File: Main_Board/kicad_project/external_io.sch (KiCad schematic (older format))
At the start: 19 parts, among them J19 I2C_BUFFERED, J20 USB_B_Micro, J21 DATA_UART, J22 I2C_EXTERNAL, U8 PCA9600DP, U9 USBLC6-2SC6

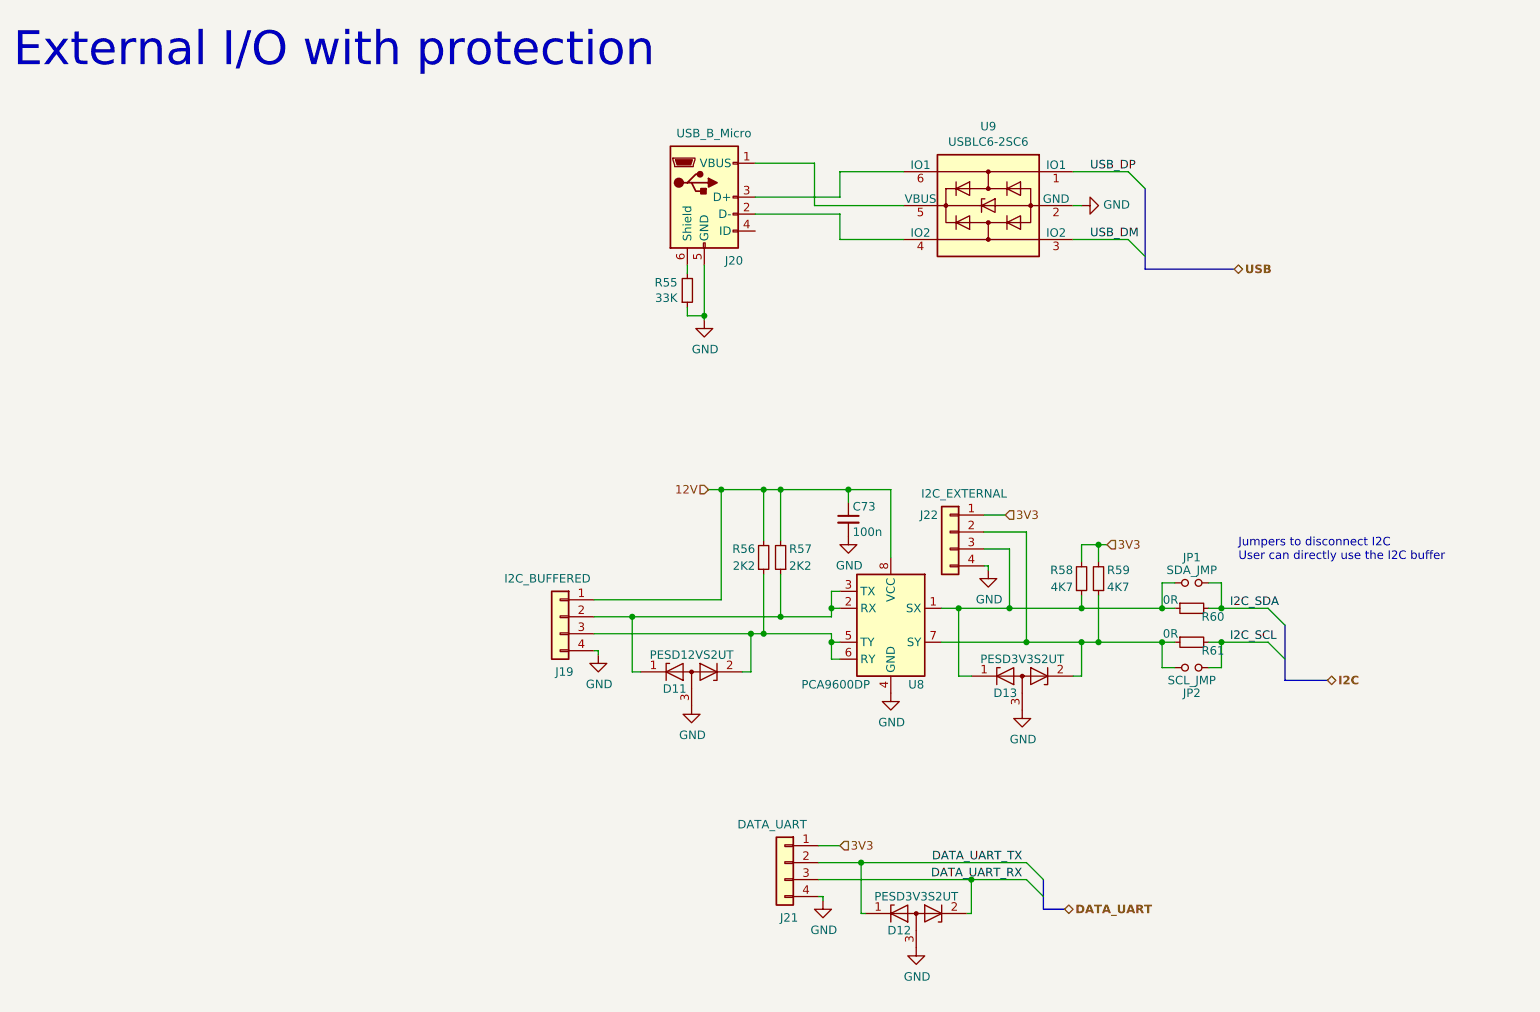
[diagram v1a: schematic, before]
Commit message: progress on MCU pinout
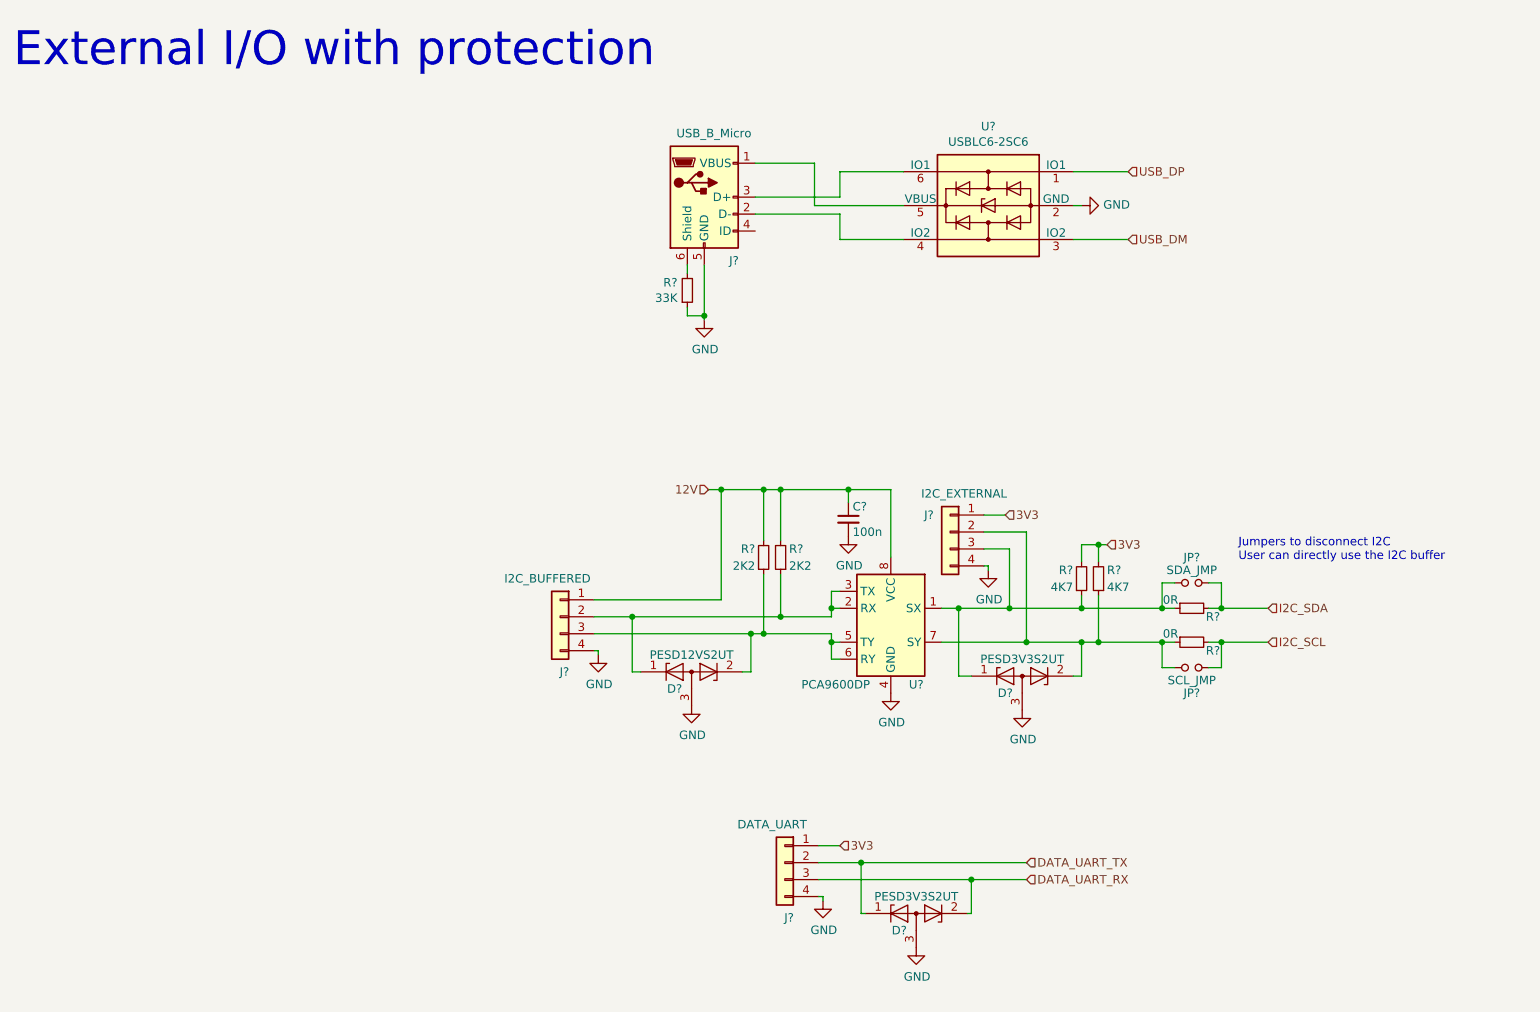
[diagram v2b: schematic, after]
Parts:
- renumbered C73 to C?, D11 to D?, D12 to D?, D13 to D?, J20 to J?, J22 to J?, J19 to J?, J21 to J?, JP1 to JP?, JP2 to JP?, R55 to R?, R60 to R?, R61 to R?, R58 to R?, R59 to R?, R57 to R?, R56 to R?, U8 to U?, U9 to U?
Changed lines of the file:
@@
 $EndDescr
 $Comp
-L Interface:PCA9600DP U8
+L Interface:PCA9600DP U?
 U 1 1 5F70BE3C
 P 5875 4200
-F 0 "U8" H 5725 3850 50  0000 C CNN
+F 0 "U?" H 5725 3850 50  0000 C CNN
 F 1 "PCA9600DP" H 6200 3850 50  0000 C CNN
 F 2 "Package_SO:TSSOP-8_3x3mm_P0.65mm" H 6675 3850 50  0001 C CNN
@@
 $EndComp
 $Comp
-L Connector:USB_B_Micro J20
+L Connector:USB_B_Micro J?
 U 1 1 5F70DEC7
 P 4775 1675
-F 0 "J20" H 4950 1300 50  0000 C CNN
+F 0 "J?" H 4950 1300 50  0000 C CNN
 F 1 "USB_B_Micro" H 4832 2051 50  0000 C CNN
 F 2 "Connector_USB:USB_Micro-B_Molex_47346-0001" H 4925 1625 50  0001 C CNN
@@
 $EndComp
 $Comp
-L LoaDy:USBLC6-2SC6 U9
+L LoaDy:USBLC6-2SC6 U?
 U 1 1 5F71A98E
 P 6450 1725
-F 0 "U9" H 6450 2192 50  0000 C CNN
+F 0 "U?" H 6450 2192 50  0000 C CNN
 F 1 "USBLC6-2SC6" H 6450 2101 50  0000 C CNN
 F 2 "Package_TO_SOT_SMD:SOT-23-6" H 7275 2125 50  0001 C CNN
@@
 $EndComp
 $Comp
-L power:GND #PWR081
+L power:GND #PWR?
 U 1 1 5F71E77C
 P 4775 2400
-F 0 "#PWR081" H 4775 2150 50  0001 C CNN
+F 0 "#PWR?" H 4775 2150 50  0001 C CNN
 F 1 "GND" H 4780 2227 50  0000 C CNN
 F 2 "" H 4775 2400 50  0001 C CNN
@@
 	5425 1725 5425 1475
 $Comp
-L Device:R_Small R55
+L Device:R_Small R?
 U 1 1 5F7222AA
 P 4675 2225
-F 0 "R55" H 4617 2179 50  0000 R CNN
+F 0 "R?" H 4617 2179 50  0000 R CNN
 F 1 "33K" H 4617 2270 50  0000 R CNN
 F 2 "Resistor_SMD:R_0603_1608Metric" H 4675 2225 50  0001 C CNN
@@
 	4675 2125 4675 2075
 $Comp
-L power:GND #PWR088
+L power:GND #PWR?
 U 1 1 5F72339E
 P 7000 1725
-F 0 "#PWR088" H 7000 1475 50  0001 C CNN
+F 0 "#PWR?" H 7000 1475 50  0001 C CNN
 F 1 "GND" V 7005 1597 50  0000 R CNN
 F 2 "" H 7000 1725 50  0001 C CNN
@@
 Wire Wire Line
 	7000 1725 6950 1725
-Entry Wire Line
-	7275 1525 7375 1625
-Entry Wire Line
-	7275 1925 7375 2025
-Wire Bus Line
-	7375 2100 7900 2100
-Text HLabel 7900 2100 2    50   BiDi ~ 10
-USB
 Wire Wire Line
 	6950 1525 7275 1525
 Wire Wire Line
 	6950 1925 7275 1925
-Text Label 7050 1925 0    50   ~ 0
-USB_DM
-Text Label 7050 1525 0    50   ~ 0
-USB_DP
-$Comp
-L Device:R_Small R60
+$Comp
+L Device:R_Small R?
 U 1 1 5F728398
 P 7650 4100
-F 0 "R60" V 7700 3975 50  0000 C CNN
+F 0 "R?" V 7700 3975 50  0000 C CNN
 F 1 "0R" V 7600 4225 50  0000 C CNN
 F 2 "Resistor_SMD:R_0603_1608Metric" H 7650 4100 50  0001 C CNN
@@
 $EndComp
 $Comp
-L Device:R_Small R61
+L Device:R_Small R?
 U 1 1 5F728F58
 P 7650 4300
-F 0 "R61" V 7700 4175 50  0000 C CNN
+F 0 "R?" V 7700 4175 50  0000 C CNN
 F 1 "0R" V 7600 4425 50  0000 C CNN
 F 2 "Resistor_SMD:R_0603_1608Metric" H 7650 4300 50  0001 C CNN
@@
 	7550 4300 7475 4300
 $Comp
-L Device:Jumper_NO_Small JP1
+L Device:Jumper_NO_Small JP?
 U 1 1 5F730E54
 P 7650 3950
-F 0 "JP1" H 7650 4100 50  0000 C CNN
+F 0 "JP?" H 7650 4100 50  0000 C CNN
 F 1 "SDA_JMP" H 7650 4025 50  0000 C CNN
 F 2 "Connector_PinHeader_2.54mm:PinHeader_1x02_P2.54mm_Vertical" H 7650 3950 50  0001 C CNN
@@
 $EndComp
 $Comp
-L Device:Jumper_NO_Small JP2
+L Device:Jumper_NO_Small JP?
 U 1 1 5F7312C9
 P 7650 4450
-F 0 "JP2" H 7650 4600 50  0000 C CNN
+F 0 "JP?" H 7650 4600 50  0000 C CNN
 F 1 "SCL_JMP" H 7650 4525 50  0000 C CNN
 F 2 "Connector_PinHeader_2.54mm:PinHeader_1x02_P2.54mm_Vertical" H 7650 4450 50  0001 C CNN
@@
 3V3
 $Comp
-L power:GND #PWR086
+L power:GND #PWR?
 U 1 1 5F72CC53
 P 6450 3875
-F 0 "#PWR086" H 6450 3625 50  0001 C CNN
+F 0 "#PWR?" H 6450 3625 50  0001 C CNN
 F 1 "GND" H 6455 3702 50  0000 C CNN
 F 2 "" H 6450 3875 50  0001 C CNN
@@
 $EndComp
 $Comp
-L Connector_Generic:Conn_01x04 J22
+L Connector_Generic:Conn_01x04 J?
 U 1 1 5F729670
 P 6225 3650
-F 0 "J22" H 6350 3750 50  0000 C CNN
+F 0 "J?" H 6350 3750 50  0000 C CNN
 F 1 "I2C_EXTERNAL" H 6143 3876 50  0000 C CNN
 F 2 "Connector_PinHeader_2.54mm:PinHeader_1x04_P2.54mm_Vertical" H 6225 3650 50  0001 C CNN
@@
 	6675 4300 7000 4300
 $Comp
-L Device:R_Small R58
+L Device:R_Small R?
 U 1 1 5F74371A
 P 7000 3925
-F 0 "R58" H 6950 3875 50  0000 R CNN
+F 0 "R?" H 6950 3875 50  0000 R CNN
 F 1 "4K7" H 6950 3975 50  0000 R CNN
 F 2 "Resistor_SMD:R_0603_1608Metric" H 7000 3925 50  0001 C CNN
@@
 $EndComp
 $Comp
-L Device:R_Small R59
+L Device:R_Small R?
 U 1 1 5F743EA7
 P 7100 3925
-F 0 "R59" H 7050 3875 50  0000 R CNN
+F 0 "R?" H 7050 3875 50  0000 R CNN
 F 1 "4K7" H 7050 3975 50  0000 R CNN
 F 2 "Resistor_SMD:R_0603_1608Metric" H 7100 3925 50  0001 C CNN
@@
 Connection ~ 7100 3725
 $Comp
-L power:GND #PWR084
+L power:GND #PWR?
 U 1 1 5F747299
 P 5875 4600
-F 0 "#PWR084" H 5875 4350 50  0001 C CNN
+F 0 "#PWR?" H 5875 4350 50  0001 C CNN
 F 1 "GND" H 5880 4427 50  0000 C CNN
 F 2 "" H 5875 4600 50  0001 C CNN
@@
 $EndComp
 $Comp
-L Connector_Generic:Conn_01x04 J19
+L Connector_Generic:Conn_01x04 J?
 U 1 1 5F7475E6
 P 3925 4150
-F 0 "J19" H 3900 3825 50  0000 C CNN
+F 0 "J?" H 3900 3825 50  0000 C CNN
 F 1 "I2C_BUFFERED" H 4000 4375 50  0000 C CNN
 F 2 "Connector_PinHeader_2.54mm:PinHeader_1x04_P2.54mm_Horizontal" H 3925 4150 50  0001 C CNN
@@
 Connection ~ 5525 4100
 $Comp
-L Device:C_Small C73
+L Device:C_Small C?
 U 1 1 5F74C7A6
 P 5625 3575
-F 0 "C73" H 5650 3650 50  0000 L CNN
+F 0 "C?" H 5650 3650 50  0000 L CNN
 F 1 "100n" H 5650 3500 50  0000 L CNN
 F 2 "Capacitor_SMD:C_0603_1608Metric" H 5625 3575 50  0001 C CNN
@@
 $EndComp
 $Comp
-L power:GND #PWR083
+L power:GND #PWR?
 U 1 1 5F74C9C7
 P 5625 3675
-F 0 "#PWR083" H 5625 3425 50  0001 C CNN
+F 0 "#PWR?" H 5625 3425 50  0001 C CNN
 F 1 "GND" H 5630 3502 50  0000 C CNN
 F 2 "" H 5625 3675 50  0001 C CNN
@@
 $EndComp
 $Comp
-L Device:R_Small R57
+L Device:R_Small R?
 U 1 1 5F74F68F
 P 5225 3800
-F 0 "R57" H 5175 3750 50  0000 R CNN
+F 0 "R?" H 5175 3750 50  0000 R CNN
 F 1 "2K2" H 5175 3850 50  0000 R CNN
 F 2 "Resistor_SMD:R_0603_1608Metric" H 5225 3800 50  0001 C CNN
@@
 $EndComp
 $Comp
-L Device:R_Small R56
+L Device:R_Small R?
 U 1 1 5F74FC84
 P 5125 3800
-F 0 "R56" H 5075 3750 50  0000 R CNN
+F 0 "R?" H 5075 3750 50  0000 R CNN
 F 1 "2K2" H 5075 3850 50  0000 R CNN
 F 2 "Resistor_SMD:R_0603_1608Metric" H 5125 3800 50  0001 C CNN
@@
 	4150 4375 4150 4350
 $Comp
-L power:GND #PWR079
+L power:GND #PWR?
 U 1 1 5F76116E
 P 4150 4375
-F 0 "#PWR079" H 4150 4125 50  0001 C CNN
+F 0 "#PWR?" H 4150 4125 50  0001 C CNN
 F 1 "GND" H 4155 4202 50  0000 C CNN
 F 2 "" H 4150 4375 50  0001 C CNN
@@
 Text HLabel 4800 3400 0    50   Input ~ 0
 12V
-Entry Wire Line
-	8100 4100 8200 4200
-Entry Wire Line
-	8100 4300 8200 4400
-Wire Bus Line
-	8200 4525 8450 4525
-Text HLabel 8450 4525 2    50   BiDi ~ 10
-I2C
-Text Label 7875 4100 0    50   ~ 0
-I2C_SDA
-Text Label 7875 4300 0    50   ~ 0
-I2C_SCL
 Wire Wire Line
 	7825 4300 8100 4300
@@
 P 4700 4475
 AR Path="/5F51A37F/5F783DBC" Ref="D?"  Part="1"
-AR Path="/5F709561/5F783DBC" Ref="D11"  Part="1"
-F 0 "D11" H 4600 4375 50  0000 C CNN
+AR Path="/5F709561/5F783DBC" Ref="D?"  Part="1"
+F 0 "D?" H 4600 4375 50  0000 C CNN
 F 1 "PESD12VS2UT" H 4700 4575 50  0000 C CNN
 F 2 "Package_TO_SOT_SMD:SOT-23" H 4700 4475 50  0001 C CNN
@@
 	4350 4150 5225 4150
 $Comp
-L power:GND #PWR080
+L power:GND #PWR?
 U 1 1 5F79653C
 P 4700 4675
-F 0 "#PWR080" H 4700 4425 50  0001 C CNN
+F 0 "#PWR?" H 4700 4425 50  0001 C CNN
 F 1 "GND" H 4705 4502 50  0000 C CNN
 F 2 "" H 4700 4675 50  0001 C CNN
@@
 $EndComp
 $Comp
-L Connector_Generic:Conn_01x04 J21
+L Connector_Generic:Conn_01x04 J?
 U 1 1 5F7AC162
 P 5250 5600
-F 0 "J21" H 5225 5275 50  0000 C CNN
+F 0 "J?" H 5225 5275 50  0000 C CNN
 F 1 "DATA_UART" H 5325 5825 50  0000 C CNN
 F 2 "Connector_PinHeader_2.54mm:PinHeader_1x04_P2.54mm_Horizontal" H 5250 5600 50  0001 C CNN
@@
 	5475 5825 5475 5800
 $Comp
-L power:GND #PWR082
+L power:GND #PWR?
 U 1 1 5F7AC5CD
 P 5475 5825
-F 0 "#PWR082" H 5475 5575 50  0001 C CNN
+F 0 "#PWR?" H 5475 5575 50  0001 C CNN
 F 1 "GND" H 5480 5652 50  0000 C CNN
 F 2 "" H 5475 5825 50  0001 C CNN
@@
 P 6025 5900
 AR Path="/5F51A37F/5F7AEF18" Ref="D?"  Part="1"
-AR Path="/5F709561/5F7AEF18" Ref="D12"  Part="1"
-F 0 "D12" H 5925 5800 50  0000 C CNN
+AR Path="/5F709561/5F7AEF18" Ref="D?"  Part="1"
+F 0 "D?" H 5925 5800 50  0000 C CNN
 F 1 "PESD3V3S2UT" H 6025 6000 50  0000 C CNN
 F 2 "Package_TO_SOT_SMD:SOT-23" H 6025 5900 50  0001 C CNN
@@
 $EndComp
 $Comp
-L power:GND #PWR085
+L power:GND #PWR?
 U 1 1 5F7AEF22
 P 6025 6100
-F 0 "#PWR085" H 6025 5850 50  0001 C CNN
+F 0 "#PWR?" H 6025 5850 50  0001 C CNN
 F 1 "GND" H 6030 5927 50  0000 C CNN
 F 2 "" H 6025 6100 50  0001 C CNN
@@
 	5700 5900 5700 5600
 Connection ~ 5700 5600
-Text Label 6650 5600 2    50   ~ 0
-DATA_UART_TX
-Text Label 6650 5700 2    50   ~ 0
-DATA_UART_RX
-Entry Wire Line
-	6675 5600 6775 5700
-Entry Wire Line
-	6675 5700 6775 5800
 Wire Wire Line
 	5700 5600 6675 5600
 Wire Wire Line
 	6350 5700 6675 5700
-Wire Bus Line
-	6775 5875 6900 5875
-Text HLabel 6900 5875 2    50   BiDi ~ 10
-DATA_UART
 Text Notes 700  925  0    200  ~ 0
 External I/O with protection
@@
 P 6650 4500
 AR Path="/5F51A37F/5F818BA4" Ref="D?"  Part="1"
-AR Path="/5F709561/5F818BA4" Ref="D13"  Part="1"
-F 0 "D13" H 6550 4400 50  0000 C CNN
+AR Path="/5F709561/5F818BA4" Ref="D?"  Part="1"
+F 0 "D?" H 6550 4400 50  0000 C CNN
 F 1 "PESD3V3S2UT" H 6650 4600 50  0000 C CNN
 F 2 "Package_TO_SOT_SMD:SOT-23" H 6650 4500 50  0001 C CNN
@@
 $EndComp
 $Comp
-L power:GND #PWR087
+L power:GND #PWR?
 U 1 1 5F818BAE
 P 6650 4700
-F 0 "#PWR087" H 6650 4450 50  0001 C CNN
+F 0 "#PWR?" H 6650 4450 50  0001 C CNN
 F 1 "GND" H 6655 4527 50  0000 C CNN
 F 2 "" H 6650 4700 50  0001 C CNN
@@
 Wire Wire Line
 	7000 4300 7100 4300
-Wire Bus Line
-	6775 5700 6775 5875
-Wire Bus Line
-	8200 4200 8200 4525
-Wire Bus Line
-	7375 1625 7375 2100
+Text HLabel 7275 1525 2    50   Input ~ 0
+USB_DP
+Text HLabel 7275 1925 2    50   Input ~ 0
+USB_DM
+Text HLabel 8100 4100 2    50   Input ~ 0
+I2C_SDA
+Text HLabel 8100 4300 2    50   Input ~ 0
+I2C_SCL
+Text HLabel 6675 5600 2    50   Input ~ 0
+DATA_UART_TX
+Text HLabel 6675 5700 2    50   Input ~ 0
+DATA_UART_RX
 $EndSCHEMATC

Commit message: schematic rev1 finished
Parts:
- gave numbers to parts that had none: 19
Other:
- note added: "I2C with 12V buffer/driver for communication\nwith the interface board."
- note added: "UART for external communication."
- note added: "USB connection with protection for MCU.\nCan serve as DFU for firmware update and\nVCom for application communication."
- moved on the sheet: C55, D1, D2, D3, J10, J11, J12, J9, JP1, JP2, R15, R16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

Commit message: main board: layout start, steppers done
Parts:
- J11, J9: footprint Connector_PinHeader_2.54mm:PinHeader_1x04_P2.54mm_Horizontal -> LoaDy:Molex_70543-0003
- J12: footprint Connector_PinHeader_2.54mm:PinHeader_1x04_P2.54mm_Vertical -> LoaDy:Molex_70543-0003
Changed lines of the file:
@@
 F 0 "J12" H 6025 3550 50  0000 C CNN
 F 1 "I2C_EXTERNAL" H 5818 3676 50  0000 C CNN
-F 2 "Connector_PinHeader_2.54mm:PinHeader_1x04_P2.54mm_Vertical" H 5900 3450 50  0001 C CNN
+F 2 "LoaDy:Molex_70543-0003" H 5900 3450 50  0001 C CNN
 F 3 "~" H 5900 3450 50  0001 C CNN
 	1    5900 3450
@@
 F 0 "J9" H 3575 3625 50  0000 C CNN
 F 1 "I2C_BUFFERED" H 3675 4175 50  0000 C CNN
-F 2 "Connector_PinHeader_2.54mm:PinHeader_1x04_P2.54mm_Horizontal" H 3600 3950 50  0001 C CNN
+F 2 "LoaDy:Molex_70543-0003" H 3600 3950 50  0001 C CNN
 F 3 "~" H 3600 3950 50  0001 C CNN
 	1    3600 3950
@@
 F 0 "J11" H 4650 5350 50  0000 C CNN
 F 1 "DATA_UART" H 4750 5900 50  0000 C CNN
-F 2 "Connector_PinHeader_2.54mm:PinHeader_1x04_P2.54mm_Horizontal" H 4675 5675 50  0001 C CNN
+F 2 "LoaDy:Molex_70543-0003" H 4675 5675 50  0001 C CNN
 F 3 "~" H 4675 5675 50  0001 C CNN
 	1    4675 5675

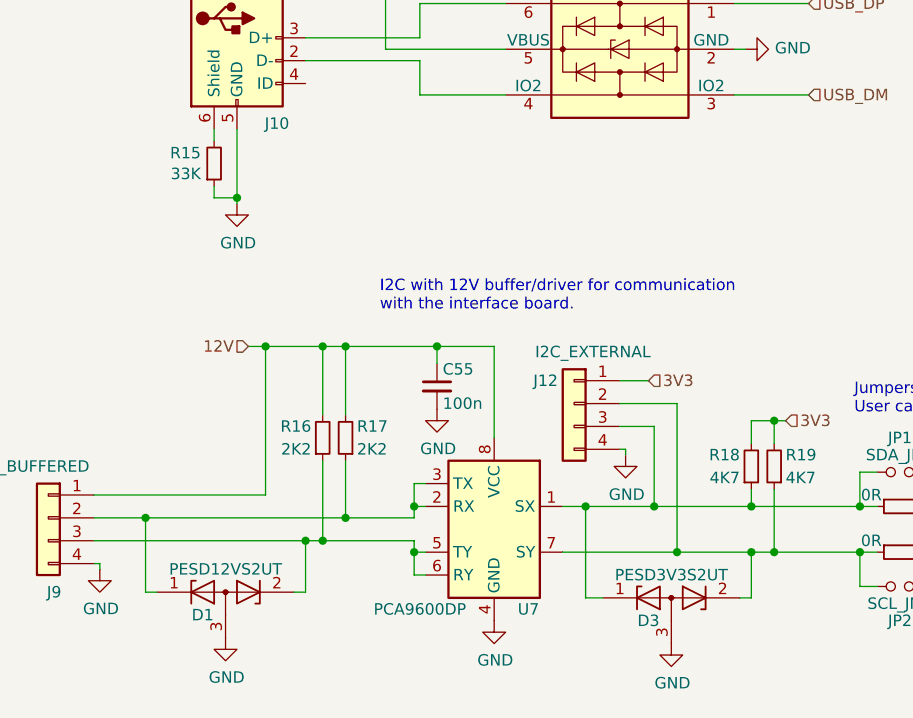
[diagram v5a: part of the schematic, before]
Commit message: external IO layout WIP, small chances to external IO schematic
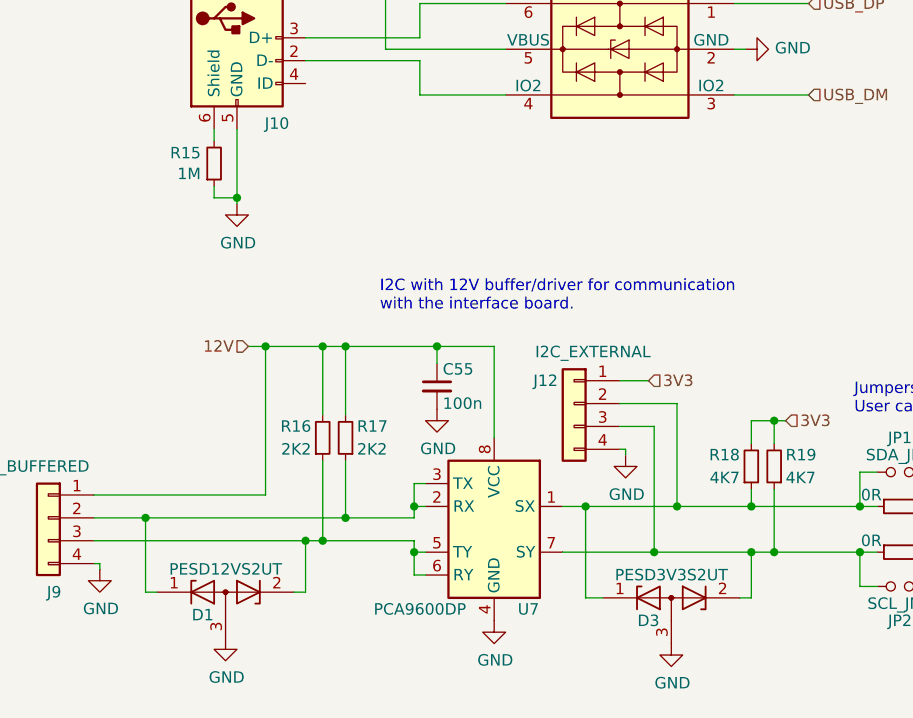
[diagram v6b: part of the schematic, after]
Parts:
- R15: value 33K -> 1M
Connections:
- net at D3.1 (K), JP1.1, R18.1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: now also J12.2 (Pin_2); no longer J12.3 (Pin_3)
- net at D3.2 (K), JP2.2, R19.1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: now also J12.3 (Pin_3); no longer J12.2 (Pin_2)
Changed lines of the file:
@@
 Sheet 7 10
 Title "Cube Main Board - External I/O"
-Date "2020-09-08"
-Rev "1"
+Date "2020-09-27"
+Rev "1.1"
 Comp "Oldřich Pecák (LoaDy)"
 Comment1 "Licensed under CERN-OHL-P v2"
@@
 P 4325 2400
 F 0 "R15" H 4267 2354 50  0000 R CNN
-F 1 "33K" H 4267 2445 50  0000 R CNN
+F 1 "1M" H 4267 2445 50  0000 R CNN
 F 2 "Resistor_SMD:R_0603_1608Metric" H 4325 2400 50  0001 C CNN
 F 3 "~" H 4325 2400 50  0001 C CNN
@@
 Connection ~ 7500 4100
 Wire Wire Line
-	6350 3450 6350 4100
-Wire Wire Line
 	6100 3450 6350 3450
-Wire Wire Line
-	6250 3550 6250 3900
 Wire Wire Line
 	6100 3550 6250 3550
@@
 	-1   0    0    -1
 $EndComp
-Connection ~ 6250 3900
-Connection ~ 6350 4100
-Wire Wire Line
-	6350 4100 5850 4100
-Wire Wire Line
-	6250 3900 6675 3900
-Wire Wire Line
-	6350 4100 6675 4100
 $Comp
 L Device:R_Small R18
@@
 	5950 4300 5950 3900
 Connection ~ 5950 3900
-Wire Wire Line
-	5950 3900 6250 3900
 Wire Wire Line
 	6625 4300 6675 4300
@@
 Text Notes 4975 5375 0    50   ~ 0
 UART for external communication.
+Wire Wire Line
+	5950 3900 6350 3900
+Wire Wire Line
+	5850 4100 6250 4100
+Wire Wire Line
+	6250 3550 6250 4100
+Connection ~ 6250 4100
+Wire Wire Line
+	6250 4100 6675 4100
+Wire Wire Line
+	6350 3450 6350 3900
+Connection ~ 6350 3900
+Wire Wire Line
+	6350 3900 6675 3900
 $EndSCHEMATC

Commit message: routing half finished
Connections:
- net USB_DM renamed USB_DATA_N
- net USB_DP renamed USB_DATA_P
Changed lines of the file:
@@
 	6675 4100 6775 4100
 Text HLabel 6925 1700 2    50   Input ~ 0
-USB_DP
+USB_DATA_P
 Text HLabel 6925 2100 2    50   Input ~ 0
-USB_DM
+USB_DATA_N
 Text HLabel 7775 3900 2    50   Input ~ 0
 I2C_SDA
